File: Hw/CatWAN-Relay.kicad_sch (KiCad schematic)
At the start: 56 parts, among them J2 INPUTS, J3 OUTPUTS, J4 I2C, J5 Serial, P1 USB_C_Plug_USB2.0, Q1 MMBT2222A, Q2 MMBT2222A, Q3 MMBT2222A, SW1 BOOT, SW2 RESET, U2 RFM95W-915-868, U3 LTV-817, U4 LTV-817, U5 LTV-817, U6 LM2596_DC-DC, U7 AP2114H-3.3TRG1, U8 ESP32-C6-WROOM-1U-N4, Y1 UD2-3NU, Y2 UD2-3NU, Y3 UD2-3NU

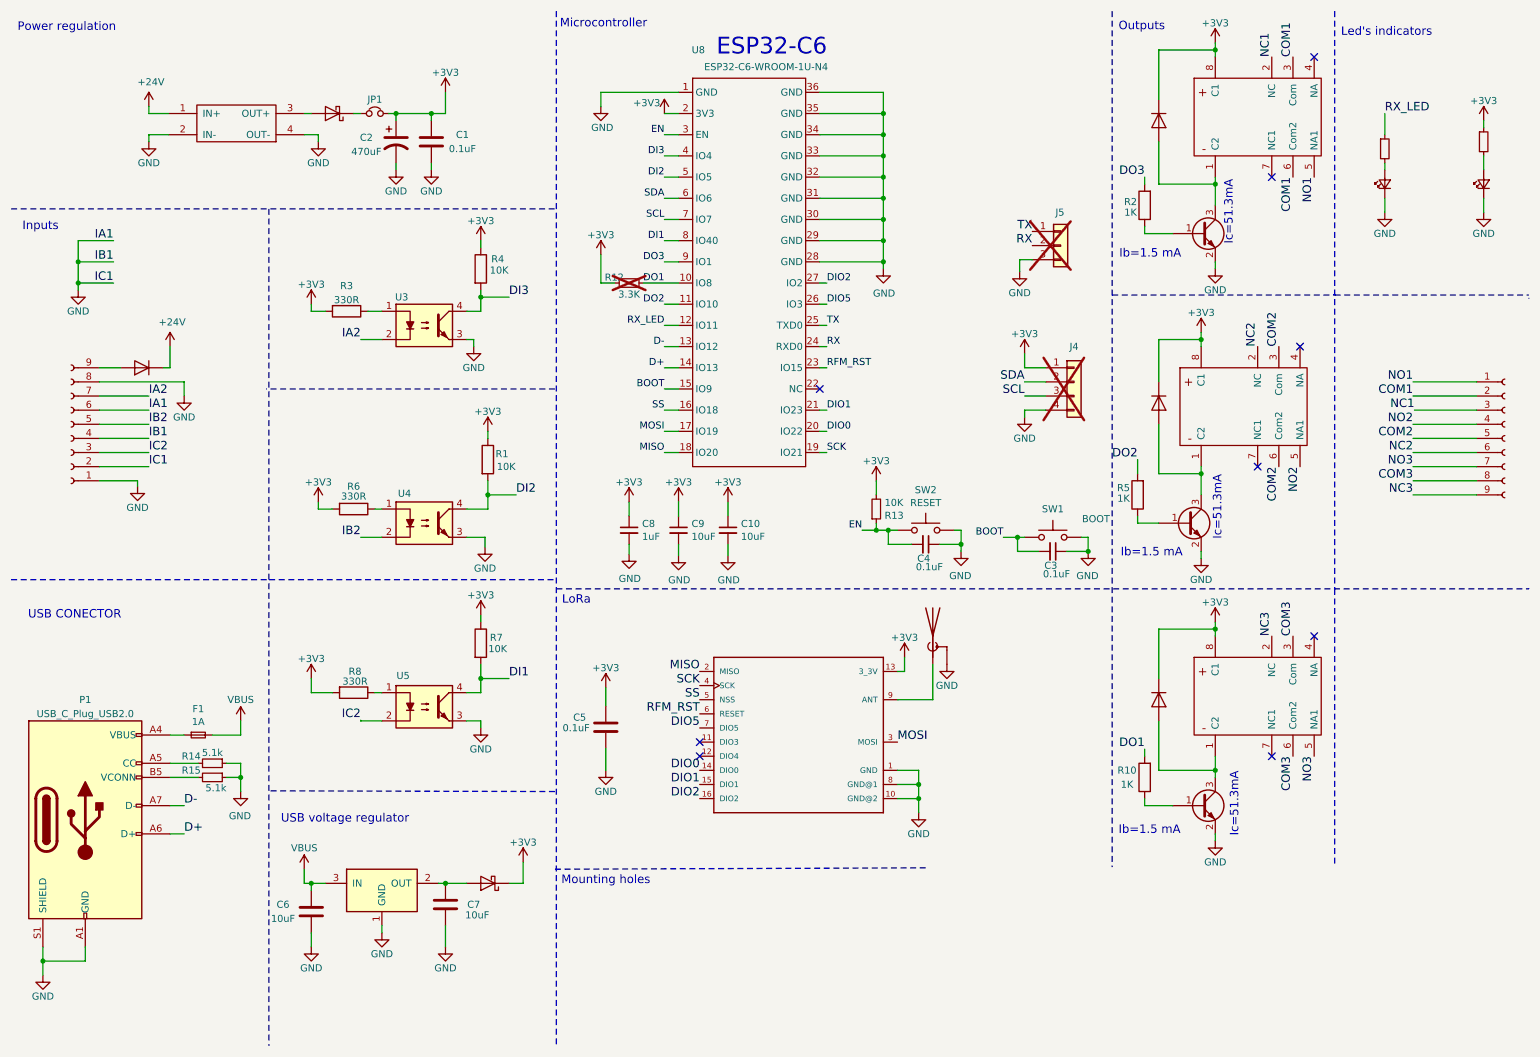
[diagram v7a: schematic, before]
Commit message: feat(hw): Change optocoupler and D1-D4 mfr# and update footprints
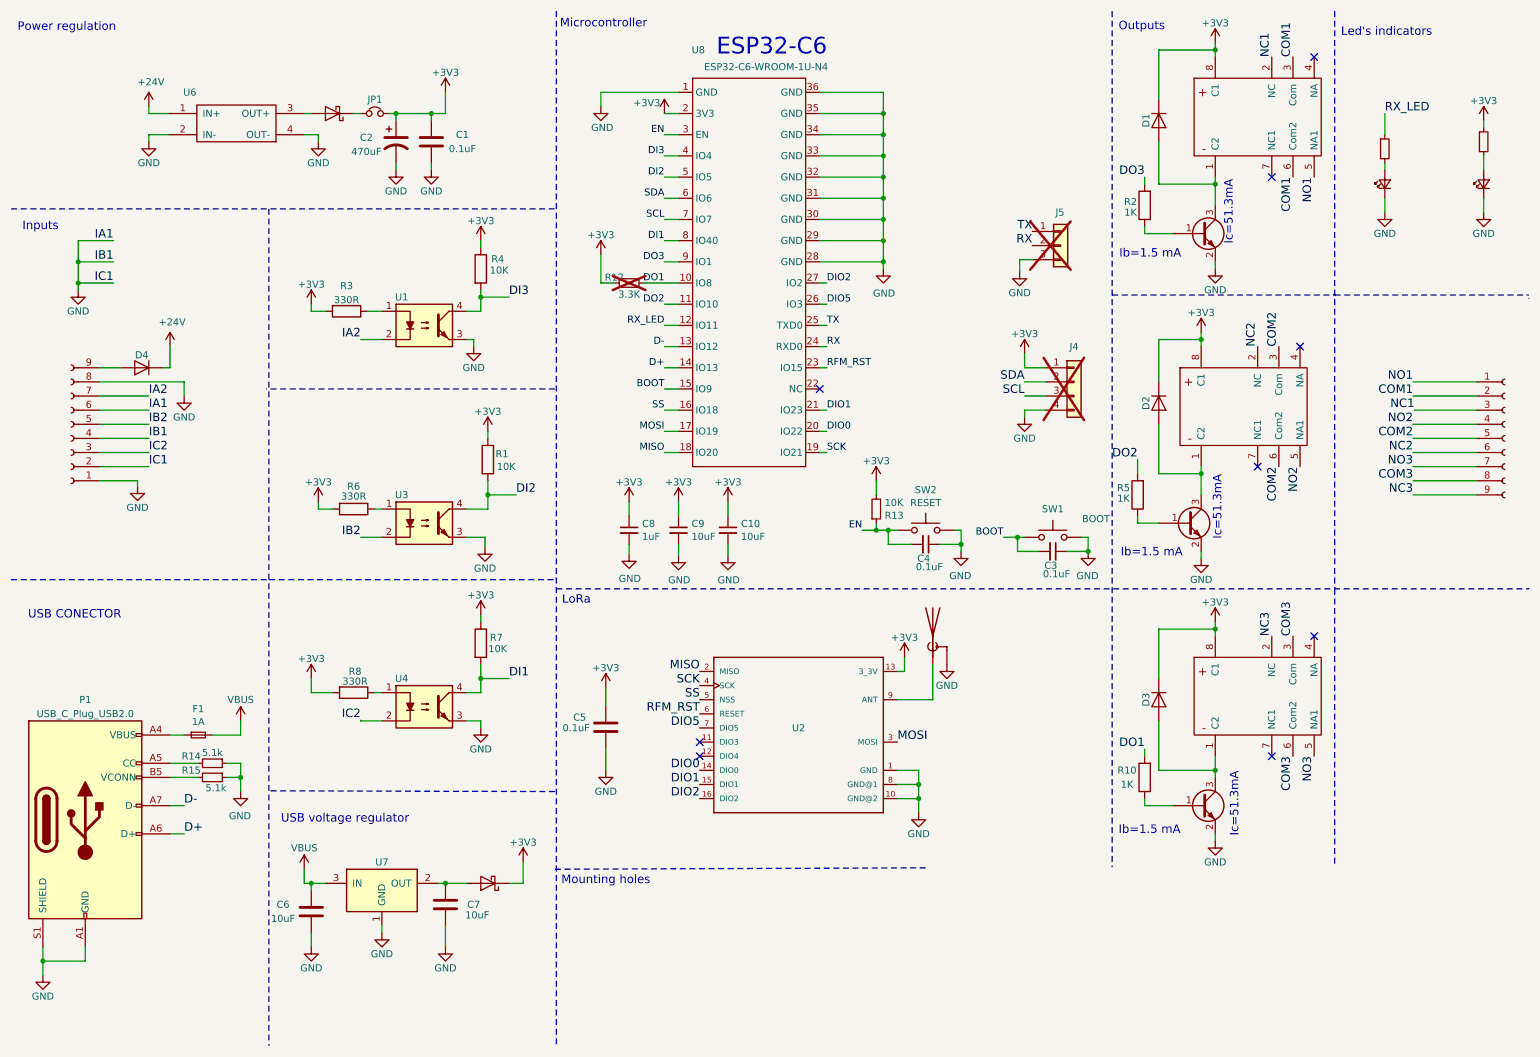
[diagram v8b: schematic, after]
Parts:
- removed U5: LTV-817, Package_DIP:DIP-4_W7.62mm_Socket, symbol CatWAN-Relay-rescue:LTV-817-agroin-rescue
- added U1: AT3H7C-CuH-S, Package_SO:SOP-4_4.4x2.6mm_P1.27mm, symbol CatWAN-Relay-rescue:LTV-817-agroin-rescue
- D1, D2, D3, D4: value RS1M -> SOD4007-MS; footprint Diode_SMD:D_SMA -> Diode_SMD:D_SOD-123F; LCSC# C513461 -> C3008061
- U3, U4: value LTV-817 -> AT3H7C-CuH-S; footprint Package_DIP:DIP-4_W7.62mm_Socket -> Package_SO:SOP-4_4.4x2.6mm_P1.27mm; LCSC# C479627 -> C20612661; manf# LTV-817 -> AT3H7C-CuH-S
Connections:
- net DI1: now also U4.4
- net DI2: now also U3.4; no longer U4.4
- net DI3: now also U1.4; no longer U3.4
- net GND: now also U1.3
- net IA2: now also U1.2; no longer U3.2
- net IB2: now also U3.2; no longer U4.2
- net IC2: now also U4.2
- net at U3.1: now also R6.1; no longer R3.1
- net at U4.1: now also R8.1; no longer R6.1
- new net: R3.1, U1.1
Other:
- moved on the sheet: U3
